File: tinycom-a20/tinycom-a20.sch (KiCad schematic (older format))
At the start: 34 parts, among them P1 CONN_02X10, P2 CONN_02X10, P3 CONN_01X01, P4 CONN_01X03, U1 ALLWINNERA10/TFBGA441, U2 H5TQG63BFR/FBGA96, Y1 Crystal_Small, Y2 Crystal_Small

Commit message: update a20+base (connect reset)
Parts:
- removed R8, R9: 47K, Resistors_SMD:R_0603, symbol R_Small
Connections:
- net labels added: LDO3_28, LDO4_28, RESET_N
- net labels removed: RESET#, UART1_RX, UART1_TX
- wire segments 277 -> 270
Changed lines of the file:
@@
 Text GLabel 850  10900 0    60   Input ~ 0
 VCC_12_INT
-Text GLabel 650  9600 0    60   Input ~ 0
-VCC_33
-$Comp
-L R_Small R8
-U 1 1 5643F633
-P 700 9700
-F 0 "R8" H 730 9720 50  0000 L CNN
-F 1 "47K" H 730 9660 50  0000 L CNN
-F 2 "Resistors_SMD:R_0603" H 700 9700 60  0001 C CNN
-F 3 "" H 700 9700 60  0000 C CNN
-	1    700  9700
-	1    0    0    -1
-$EndComp
-$Comp
-L R_Small R9
-U 1 1 5643FBFC
-P 850 9700
-F 0 "R9" H 880 9720 50  0000 L CNN
-F 1 "47K" H 880 9660 50  0000 L CNN
-F 2 "Resistors_SMD:R_0603" H 850 9700 60  0001 C CNN
-F 3 "" H 850 9700 60  0000 C CNN
-	1    850  9700
-	1    0    0    -1
-$EndComp
 Text GLabel 19500 8100 0    60   Input ~ 0
 VCC_33
@@
 Text GLabel 1100 9150 0    60   Input ~ 0
 UBOOT_SEL
-Text GLabel 700  9900 0    60   Input ~ 0
-RESET#
-Text GLabel 600  9750 0    60   Input ~ 0
+Text GLabel 900  9800 0    60   Input ~ 0
+RESET_N
+Text GLabel 900  9700 0    60   Input ~ 0
 NMI_N
 Text GLabel 10350 8450 2    60   Input ~ 0
@@
 Text GLabel 19100 10500 0    60   Input ~ 0
 HSCL
-Text GLabel 20950 10350 0    60   Input ~ 0
-UART1_TX
-Text GLabel 20950 10250 0    60   Input ~ 0
-UART1_RX
 Text GLabel 19600 10100 2    60   Input ~ 0
 MICIN1
@@
 VCC_12_CPU
 $Comp
-L GND #PWR029
+L GND #PWR028
 U 1 1 567EBA12
 P 18900 9250
-F 0 "#PWR029" H 18900 9000 50  0001 C CNN
+F 0 "#PWR028" H 18900 9000 50  0001 C CNN
 F 1 "GND" H 18900 9100 50  0000 C CNN
 F 2 "" H 18900 9250 60  0000 C CNN
@@
 VCC_12_INT
 $Comp
-L GND #PWR030
+L GND #PWR029
 U 1 1 5685339B
 P 21450 8250
-F 0 "#PWR030" H 21450 8000 50  0001 C CNN
+F 0 "#PWR029" H 21450 8000 50  0001 C CNN
 F 1 "GND" H 21450 8100 50  0000 C CNN
 F 2 "" H 21450 8250 60  0000 C CNN
@@
 Connection ~ 950  9500
 Wire Wire Line
-	1050 9800 950  9800
-Wire Wire Line
-	950  9800 950  9900
-Wire Wire Line
-	950  9900 700  9900
-Wire Wire Line
-	700  9900 700  9800
+	900  9800 1050 9800
 Wire Wire Line
 	1050 9700 900  9700
-Wire Wire Line
-	900  9700 900  9800
-Wire Wire Line
-	900  9800 600  9800
-Wire Wire Line
-	650  9600 850  9600
-Connection ~ 700  9600
 Wire Wire Line
 	19500 8100 19500 8350
@@
 Wire Wire Line
 	1100 9200 1100 9050
-Wire Wire Line
-	600  9800 600  9750
-Connection ~ 850  9800
 Wire Wire Line
 	9950 8450 9050 8450
@@
 HSCL
 $Comp
-L GND #PWR?
+L GND #PWR030
 U 1 1 56B096CE
 P 6100 13700
-F 0 "#PWR?" H 6100 13450 50  0001 C CNN
+F 0 "#PWR030" H 6100 13450 50  0001 C CNN
 F 1 "GND" H 6100 13550 50  0000 C CNN
 F 2 "" H 6100 13700 50  0000 C CNN
@@
 Text GLabel 1050 13700 0    60   Input ~ 0
 HPOUTL
+Text GLabel 21450 9850 2    60   Input ~ 0
+RESET_N
+Text GLabel 20950 10150 0    60   Input ~ 0
+LDO3_28
+Text GLabel 20950 10250 0    60   Input ~ 0
+LDO4_28
 $EndSCHEMATC

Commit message: start add i2s to a20
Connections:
- net labels added: I2S_LRCK, I2S_SCK, I2S_SD
- net labels removed: HPOUTL, HPOUTR, MICIN1
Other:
- note added: "TODO: check this! (i2s_sck)"
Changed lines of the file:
@@
 NoConn ~ 7050 12150
 NoConn ~ 7050 12250
-NoConn ~ 7050 12350
 NoConn ~ 7050 12450
-NoConn ~ 7050 12550
 NoConn ~ 7050 12650
 NoConn ~ 7050 12750
 NoConn ~ 7050 12850
 NoConn ~ 7050 12950
-NoConn ~ 7050 13050
 NoConn ~ 7050 13150
 NoConn ~ 7050 13250
@@
 HSCL
 Text GLabel 19600 10100 2    60   Input ~ 0
-MICIN1
+I2S_SCK
 Text GLabel 19600 10400 2    60   Input ~ 0
 HHPD
@@
 VCC_33
 Text GLabel 19600 10200 2    60   Input ~ 0
-HPOUTL
+I2S_SD
 Text GLabel 19600 10300 2    60   Input ~ 0
-HPOUTR
-Text GLabel 1050 12600 0    60   Input ~ 0
-MICIN1
+I2S_LRCK
 Wire Wire Line
 	300  13400 300  13450
-Text GLabel 1050 13600 0    60   Input ~ 0
-HPOUTR
-Text GLabel 1050 13700 0    60   Input ~ 0
-HPOUTL
 Text GLabel 21450 9850 2    60   Input ~ 0
 RESET_N
@@
 Text GLabel 20950 10250 0    60   Input ~ 0
 LDO4_28
+NoConn ~ 1050 12600
+NoConn ~ 1050 13600
+NoConn ~ 1050 13700
+Text GLabel 7050 12550 0    60   Input ~ 0
+I2S_LRCK
+Text GLabel 7050 13050 0    60   Input ~ 0
+I2S_SD
+Text GLabel 7050 12350 0    60   Input ~ 0
+I2S_SCK
+Text Notes 6150 11750 0    60   ~ 0
+TODO: check this! (i2s_sck)
 $EndSCHEMATC

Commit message: start add cam to a20
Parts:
- added P5: CONN_02X12, tinycom:fpc24, symbol CONN_02X12
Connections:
- net labels added: CSI0_D0, CSI0_D1, CSI0_D2, CSI0_D3, CSI0_D4, CSI0_D5, CSI0_D6, CSI0_D7
- no-connect marks 209 -> 201
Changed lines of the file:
@@
 NoConn ~ 5850 3150
 NoConn ~ 5850 3250
-NoConn ~ 5850 3350
-NoConn ~ 5850 3450
-NoConn ~ 5850 3550
-NoConn ~ 5850 3650
-NoConn ~ 5850 3750
-NoConn ~ 5850 3850
-NoConn ~ 5850 3950
-NoConn ~ 5850 4050
 NoConn ~ 5850 4950
 NoConn ~ 5850 5050
@@
 Text Notes 6150 11750 0    60   ~ 0
 TODO: check this! (i2s_sck)
+$Comp
+L CONN_02X12 P5
+U 1 1 572DCF42
+P 20250 12300
+F 0 "P5" H 20250 12950 50  0000 C CNN
+F 1 "CONN_02X12" V 20250 12300 50  0000 C CNN
+F 2 "tinycom:fpc24" H 20250 11100 50  0000 C CNN
+F 3 "" H 20250 11100 50  0000 C CNN
+	1    20250 12300
+	1    0    0    -1
+$EndComp
+Text GLabel 20500 11850 2    60   Input ~ 0
+CSI0_D1
+Text GLabel 20000 11950 0    60   Input ~ 0
+CSI0_D3
+Text GLabel 20000 12150 0    60   Input ~ 0
+CSI0_D0
+Text GLabel 20500 12150 2    60   Input ~ 0
+CSI0_D2
+Text GLabel 20500 12850 2    60   Input ~ 0
+CSI0_D4
+Text GLabel 20000 12850 0    60   Input ~ 0
+CSI0_D6
+Text GLabel 20000 12650 0    60   Input ~ 0
+CSI0_D5
+Text GLabel 20500 12550 2    60   Input ~ 0
+CSI0_D7
+Text GLabel 5850 3350 2    60   Input ~ 0
+CSI0_D0
+Text GLabel 5850 3450 2    60   Input ~ 0
+CSI0_D1
+Text GLabel 5850 3550 2    60   Input ~ 0
+CSI0_D2
+Text GLabel 5850 3650 2    60   Input ~ 0
+CSI0_D3
+Text GLabel 5850 3750 2    60   Input ~ 0
+CSI0_D4
+Text GLabel 5850 3850 2    60   Input ~ 0
+CSI0_D5
+Text GLabel 5850 3950 2    60   Input ~ 0
+CSI0_D6
+Text GLabel 5850 4050 2    60   Input ~ 0
+CSI0_D7
 $EndSCHEMATC

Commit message: a20 route cam,hdmi,i2s
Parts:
- removed P5: CONN_02X12, tinycom:fpc24, symbol CONN_02X12
- added U3: fpc24, tinycom:fpc24, symbol fpc24
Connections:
- net labels added: CSI0_HSYNC, CSI0_MCLK, CSI0_PCLK, CSI0_VSYNC, TWI1_SCK, TWI1_SDA
- wire segments 270 -> 274
- no-connect marks 201 -> 196

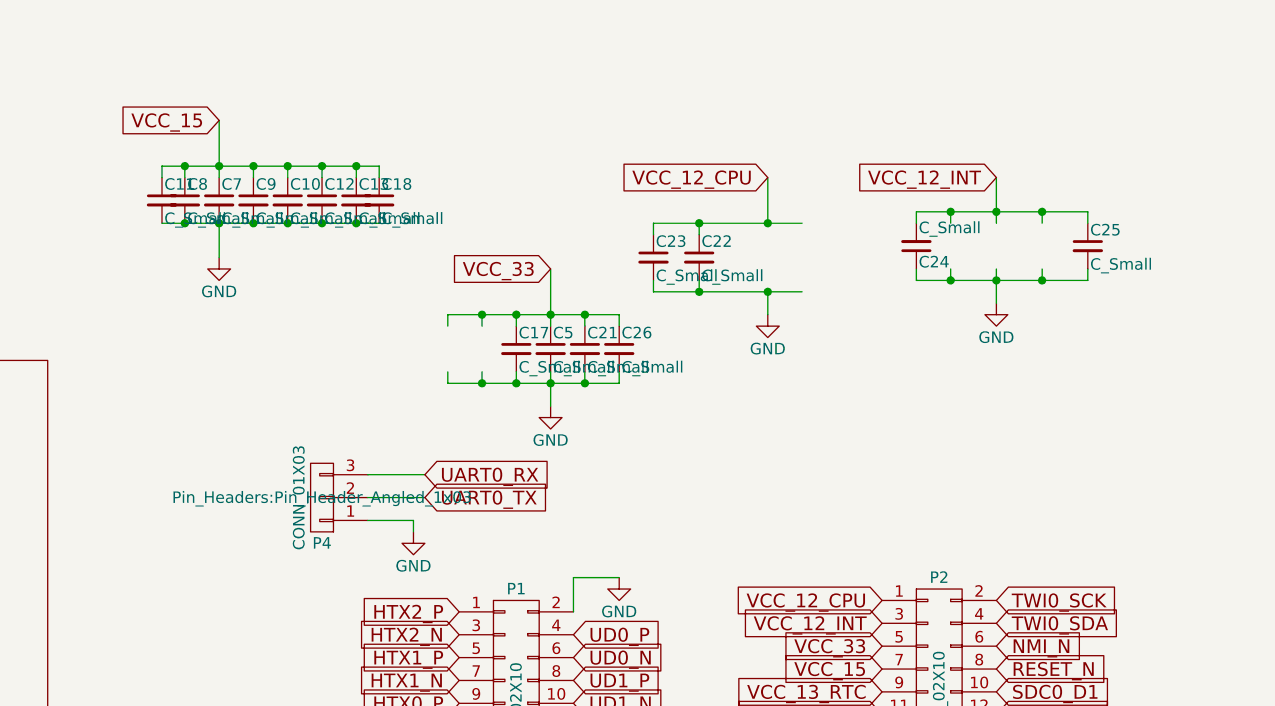
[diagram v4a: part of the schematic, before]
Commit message: a20 move caps
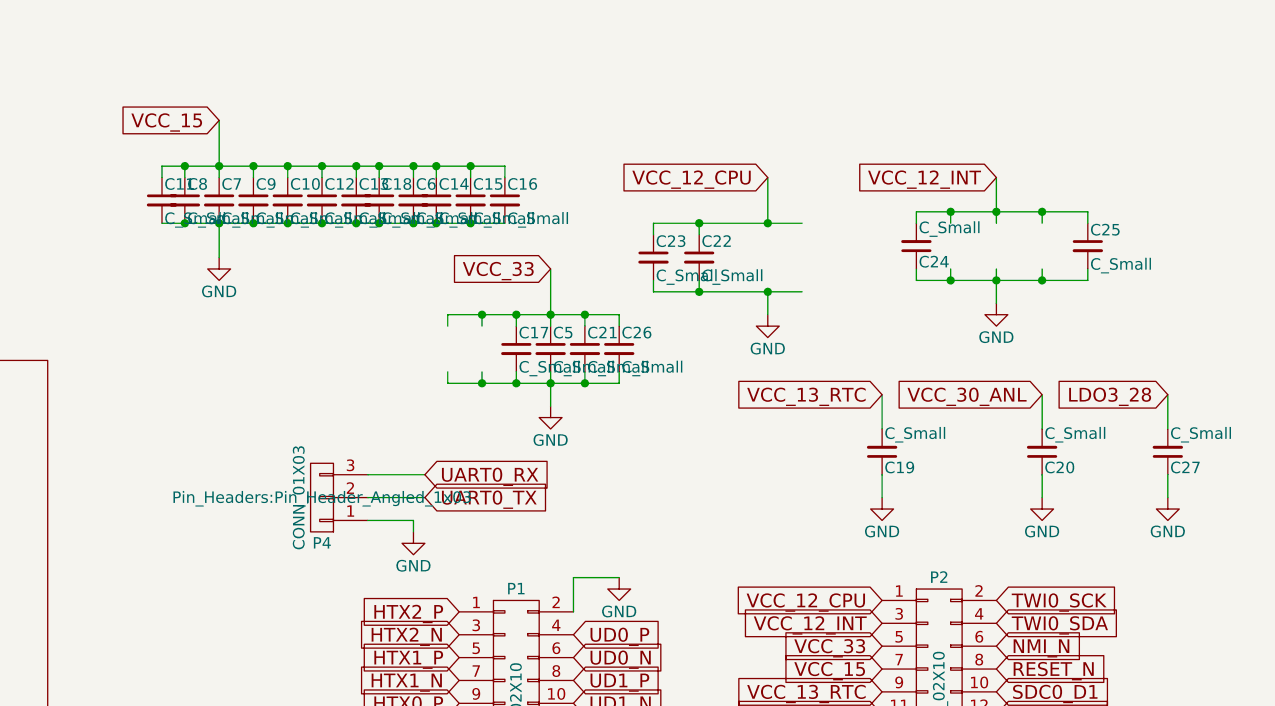
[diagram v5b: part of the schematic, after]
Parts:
- added C14, C15, C16, C19, C20, C27, C6: C_Small, Capacitors_SMD:C_0603, symbol C_Small
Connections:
- wire segments 274 -> 284

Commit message: a20 pics
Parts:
- added C28: C_Small, Capacitors_SMD:C_0603, symbol C_Small
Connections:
- wire segments 284 -> 288
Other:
- moved on the sheet: C14, C6
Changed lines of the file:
@@
 L C_Small C6
 U 1 1 573FCDA4
-P 18900 7800
-F 0 "C6" H 18910 7870 50  0000 L CNN
-F 1 "C_Small" H 18910 7720 50  0000 L CNN
-F 2 "Capacitors_SMD:C_0603" H 18900 7800 60  0001 C CNN
-F 3 "" H 18900 7800 60  0000 C CNN
-	1    18900 7800
+P 20600 8050
+F 0 "C6" H 20610 8120 50  0000 L CNN
+F 1 "C_Small" H 20610 7970 50  0000 L CNN
+F 2 "Capacitors_SMD:C_0603" H 20600 8050 60  0001 C CNN
+F 3 "" H 20600 8050 60  0000 C CNN
+	1    20600 8050
 	1    0    0    -1
 $EndComp
@@
 L C_Small C14
 U 1 1 573FCE28
-P 19000 7800
-F 0 "C14" H 19010 7870 50  0000 L CNN
-F 1 "C_Small" H 19010 7720 50  0000 L CNN
-F 2 "Capacitors_SMD:C_0603" H 19000 7800 60  0001 C CNN
-F 3 "" H 19000 7800 60  0000 C CNN
-	1    19000 7800
+P 21450 8000
+F 0 "C14" H 21460 8070 50  0000 L CNN
+F 1 "C_Small" H 21460 7920 50  0000 L CNN
+F 2 "Capacitors_SMD:C_0603" H 21450 8000 60  0001 C CNN
+F 3 "" H 21450 8000 60  0000 C CNN
+	1    21450 8000
 	1    0    0    -1
 $EndComp
@@
 Wire Wire Line
 	22200 9000 22200 9100
+$Comp
+L C_Small C28
+U 1 1 573FFFBE
+P 13900 5750
+F 0 "C28" H 13910 5820 50  0000 L CNN
+F 1 "C_Small" H 13910 5670 50  0000 L CNN
+F 2 "Capacitors_SMD:C_0603" H 13900 5750 60  0001 C CNN
+F 3 "" H 13900 5750 60  0000 C CNN
+	1    13900 5750
+	1    0    0    -1
+$EndComp
+Wire Wire Line
+	13900 5650 13900 5550
+Connection ~ 13900 5550
+Wire Wire Line
+	13900 5850 13600 5850
+Connection ~ 13600 5850
+Wire Wire Line
+	20600 7900 20600 7950
+Wire Wire Line
+	20600 8200 20600 8150
 $EndSCHEMATC

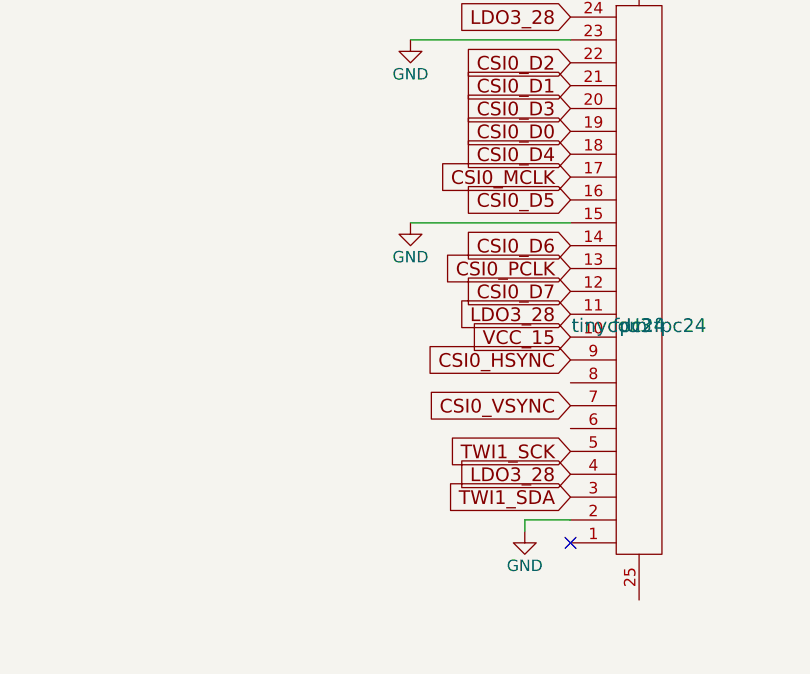
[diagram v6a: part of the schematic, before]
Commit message: a20: fix CSI routing
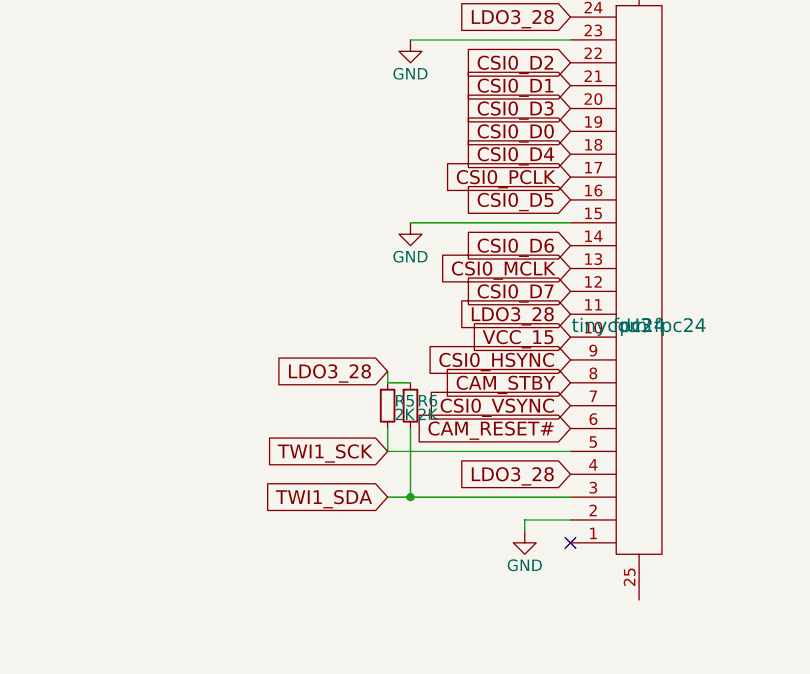
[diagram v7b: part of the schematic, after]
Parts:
- added R5, R6: 2K, Resistors_SMD:R_0603, symbol R_Small
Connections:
- net labels added: CAM_RESET#, CAM_STBY
- wire segments 288 -> 294
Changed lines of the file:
@@
 CSI0_VSYNC
 Text GLabel 21600 12500 0    60   Input ~ 0
+CSI0_PCLK
+Text GLabel 21600 12900 0    60   Input ~ 0
 CSI0_MCLK
-Text GLabel 21600 12900 0    60   Input ~ 0
-CSI0_PCLK
 Text GLabel 7050 13750 0    60   Input ~ 0
 TWI1_SCK
 Text GLabel 7050 13850 0    60   Input ~ 0
 TWI1_SDA
-Text GLabel 21600 13700 0    60   Input ~ 0
+Text GLabel 20800 13700 0    60   Input ~ 0
 TWI1_SCK
-Text GLabel 21600 13900 0    60   Input ~ 0
+Text GLabel 20800 13900 0    60   Input ~ 0
 TWI1_SDA
 $Comp
@@
 Wire Wire Line
 	20600 8200 20600 8150
+Wire Wire Line
+	21600 13900 20800 13900
+Wire Wire Line
+	21600 13700 20800 13700
+Text GLabel 21600 13600 0    60   Input ~ 0
+CAM_RESET#
+Text GLabel 21600 13400 0    60   Input ~ 0
+CAM_STBY
+Text GLabel 20800 13350 0    60   Input ~ 0
+LDO3_28
+$Comp
+L R_Small R5
+U 1 1 5740386C
+P 20800 13500
+F 0 "R5" H 20830 13520 50  0000 L CNN
+F 1 "2K" H 20830 13460 50  0000 L CNN
+F 2 "Resistors_SMD:R_0603" H 20800 13500 60  0001 C CNN
+F 3 "" H 20800 13500 60  0000 C CNN
+	1    20800 13500
+	1    0    0    -1
+$EndComp
+$Comp
+L R_Small R6
+U 1 1 57403CC8
+P 20900 13500
+F 0 "R6" H 20930 13520 50  0000 L CNN
+F 1 "2K" H 20930 13460 50  0000 L CNN
+F 2 "Resistors_SMD:R_0603" H 20900 13500 60  0001 C CNN
+F 3 "" H 20900 13500 60  0000 C CNN
+	1    20900 13500
+	1    0    0    -1
+$EndComp
+Wire Wire Line
+	20800 13350 20800 13400
+Wire Wire Line
+	20800 13400 20900 13400
+Wire Wire Line
+	20800 13700 20800 13600
+Wire Wire Line
+	20900 13600 20900 13900
+Connection ~ 20900 13900
 $EndSCHEMATC

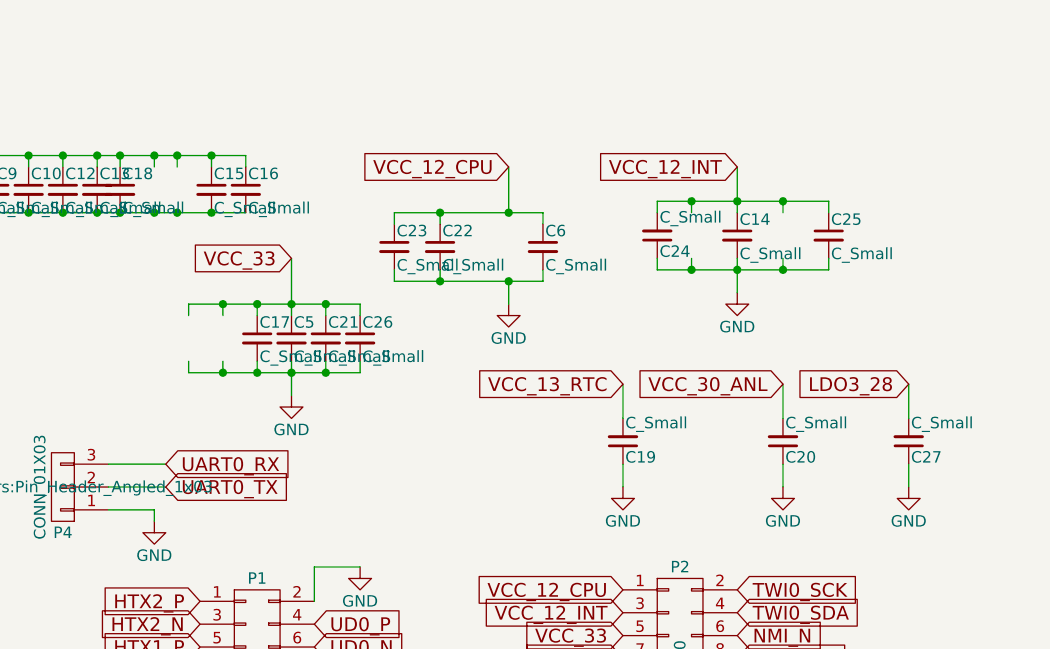
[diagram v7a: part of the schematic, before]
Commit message: a20: add caps for camera
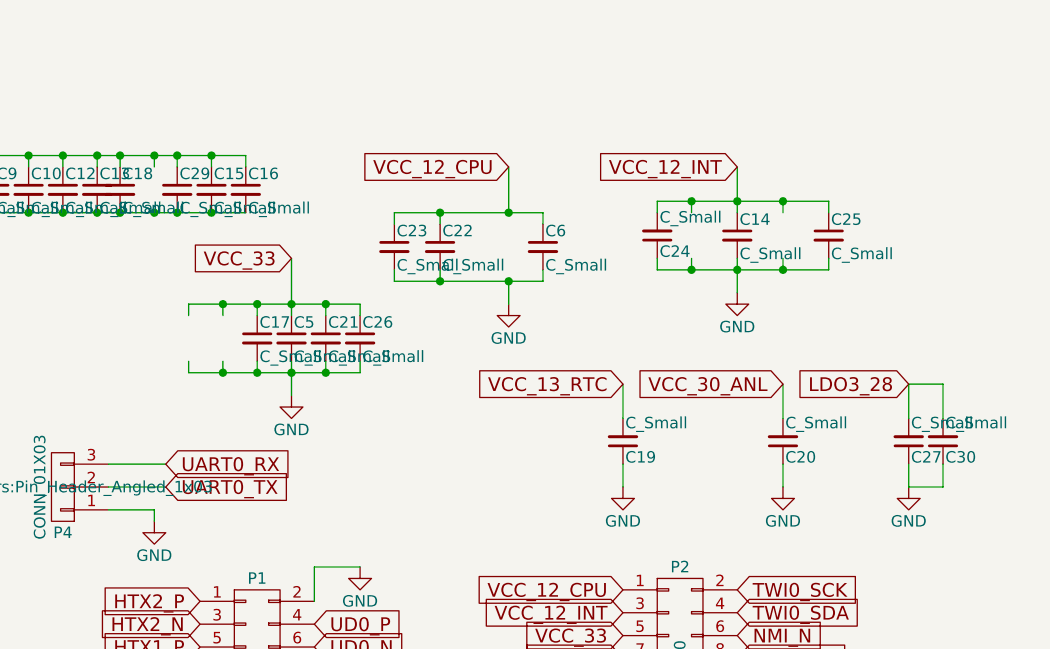
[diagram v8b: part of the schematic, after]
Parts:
- added C29, C30: C_Small, Capacitors_SMD:C_0603, symbol C_Small
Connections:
- wire segments 294 -> 298
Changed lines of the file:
@@
 	20900 13600 20900 13900
 Connection ~ 20900 13900
+$Comp
+L C_Small C29
+U 1 1 57404764
+P 19000 7800
+F 0 "C29" H 19010 7870 50  0000 L CNN
+F 1 "C_Small" H 19010 7720 50  0000 L CNN
+F 2 "Capacitors_SMD:C_0603" H 19000 7800 60  0001 C CNN
+F 3 "" H 19000 7800 60  0000 C CNN
+	1    19000 7800
+	1    0    0    -1
+$EndComp
+$Comp
+L C_Small C30
+U 1 1 57404FAF
+P 22350 8900
+F 0 "C30" H 22360 8970 50  0000 L CNN
+F 1 "C_Small" H 22360 8820 50  0000 L CNN
+F 2 "Capacitors_SMD:C_0603" H 22350 8900 60  0001 C CNN
+F 3 "" H 22350 8900 60  0000 C CNN
+	1    22350 8900
+	1    0    0    1
+$EndComp
+Wire Wire Line
+	22200 8650 22350 8650
+Wire Wire Line
+	22350 8650 22350 8800
+Wire Wire Line
+	22350 9000 22350 9100
+Wire Wire Line
+	22350 9100 22200 9100
 $EndSCHEMATC
